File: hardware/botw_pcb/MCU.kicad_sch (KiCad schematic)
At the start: 12 parts, among them J1 Conn_02x03_Odd_Even, J2 Conn_01x03, U3 STM32F030CCTx, U4 MC6470

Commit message: Added pullups to I2C'
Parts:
- added R19, R20: 4k7, Resistor_SMD:R_0603_1608Metric, symbol Device:R_Small_US
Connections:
- net +3.3V: now also R19.2, R20.2
- net SCL: now also R19.1
- net SDA: now also R20.1
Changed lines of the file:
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@@
   (junction (at 180.34 71.12) (diameter 0) (color 0 0 0 0)
   )
+  (junction (at 218.44 134.62) (diameter 0) (color 0 0 0 0)
+  )
   (junction (at 167.64 71.12) (diameter 0) (color 0 0 0 0)
   )
@@
   (junction (at 135.89 139.7) (diameter 0) (color 0 0 0 0)
   )
-  (bus_entry (at 236.22 59.69) (size 2.54 2.54)
-    (stroke (width 0) (type default) (color 0 0 0 0))
-  )
   (bus_entry (at 519.43 19.05) (size 2.54 2.54)
     (stroke (width 0) (type default) (color 0 0 0 0))
@@
     (stroke (width 0) (type default) (color 0 0 0 0))
   )
+  (wire (pts (xy 218.44 134.62) (xy 218.44 137.16))
+    (stroke (width 0) (type default) (color 0 0 0 0))
+  )
+  (wire (pts (xy 222.25 130.81) (xy 222.25 134.62))
+    (stroke (width 0) (type default) (color 0 0 0 0))
+  )
   (wire (pts (xy 135.89 139.7) (xy 133.35 139.7))
     (stroke (width 0) (type default) (color 0 0 0 0))
@@
     (stroke (width 0) (type default) (color 0 0 0 0))
   )
+  (wire (pts (xy 218.44 133.35) (xy 218.44 134.62))
+    (stroke (width 0) (type default) (color 0 0 0 0))
+  )
   (wire (pts (xy 152.4 127) (xy 151.13 127))
     (stroke (width 0) (type default) (color 0 0 0 0))
@@
     (stroke (width 0) (type default) (color 0 0 0 0))
   )
+  (wire (pts (xy 218.44 134.62) (xy 222.25 134.62))
+    (stroke (width 0) (type default) (color 0 0 0 0))
+  )
   (wire (pts (xy 133.35 142.24) (xy 133.35 139.7))
     (stroke (width 0) (type default) (color 0 0 0 0))
@@
     )
   )
+  (global_label "SDA" (shape input) (at 213.36 137.16 180) (fields_autoplaced)
+    (effects (font (size 1.27 1.27)) (justify right))
+    (property "Intersheet References" "${INTERSHEET_REFS}" (id 0) (at 207.3788 137.0806 0)
+      (effects (font (size 1.27 1.27)) (justify right) hide)
+    )
+  )
   (global_label "SWDIO" (shape input) (at 189.23 123.19 0) (fields_autoplaced)
     (effects (font (size 1.27 1.27)) (justify left))
@@
     (effects (font (size 1.27 1.27)) (justify right))
     (property "Intersheet References" "${INTERSHEET_REFS}" (id 0) (at 108.1374 124.5394 0)
+      (effects (font (size 1.27 1.27)) (justify right) hide)
+    )
+  )
+  (global_label "SCL" (shape input) (at 213.36 133.35 180) (fields_autoplaced)
+    (effects (font (size 1.27 1.27)) (justify right))
+    (property "Intersheet References" "${INTERSHEET_REFS}" (id 0) (at 207.4393 133.4294 0)
       (effects (font (size 1.27 1.27)) (justify right) hide)
     )
@@
     (pin "1")
     (pin "2")
+  )
+  (symbol (lib_id "power:+3.3V") (at 222.25 130.81 0) (unit 1)
+    (in_bom yes) (on_board yes)
+    (property "Reference" "#PWR0153" (id 0) (at 222.25 134.62 0)
+      (effects (font (size 1.27 1.27)) hide)
+    )
+    (property "Value" "+3.3V" (id 1) (at 215.9 128.27 0)
+      (effects (font (size 1.27 1.27)) (justify left))
+    )
+    (property "Footprint" "" (id 2) (at 222.25 130.81 0)
+      (effects (font (size 1.27 1.27)) hide)
+    )
+    (property "Datasheet" "" (id 3) (at 222.25 130.81 0)
+      (effects (font (size 1.27 1.27)) hide)
+    )
+    (pin "1")
   )
   (symbol (lib_id "power:+3.3V") (at 243.84 111.76 0) (unit 1)
@@
     (pin "1")
   )
+  (symbol (lib_id "Device:R_Small_US") (at 215.9 137.16 90) (unit 1)
+    (in_bom yes) (on_board yes)
+    (property "Reference" "R20" (id 0) (at 215.9 142.24 90))
+    (property "Value" "4k7" (id 1) (at 215.9 139.7 90))
+    (property "Footprint" "Resistor_SMD:R_0603_1608Metric" (id 2) (at 215.9 137.16 0)
+      (effects (font (size 1.27 1.27)) hide)
+    )
+    (property "Datasheet" "~" (id 3) (at 215.9 137.16 0)
+      (effects (font (size 1.27 1.27)) hide)
+    )
+    (pin "1")
+    (pin "2")
+  )
   (symbol (lib_id "Device:R_Small_US") (at 102.87 104.14 0) (unit 1)
     (in_bom yes) (on_board yes) (fields_autoplaced)
@@
       (effects (font (size 1.27 1.27)) hide)
     )
+    (pin "1")
+    (pin "2")
+  )
+  (symbol (lib_id "Device:R_Small_US") (at 215.9 133.35 90) (unit 1)
+    (in_bom yes) (on_board yes) (fields_autoplaced)
+    (property "Reference" "R19" (id 0) (at 215.9 127 90))
+    (property "Value" "4k7" (id 1) (at 215.9 129.54 90))
+    (property "Footprint" "Resistor_SMD:R_0603_1608Metric" (id 2) (at 215.9 133.35 0)
+      (effects (font (size 1.27 1.27)) hide)
+    )
+    (property "Datasheet" "~" (id 3) (at 215.9 133.35 0)
+      (effects (font (size 1.27 1.27)) hide)
+    )

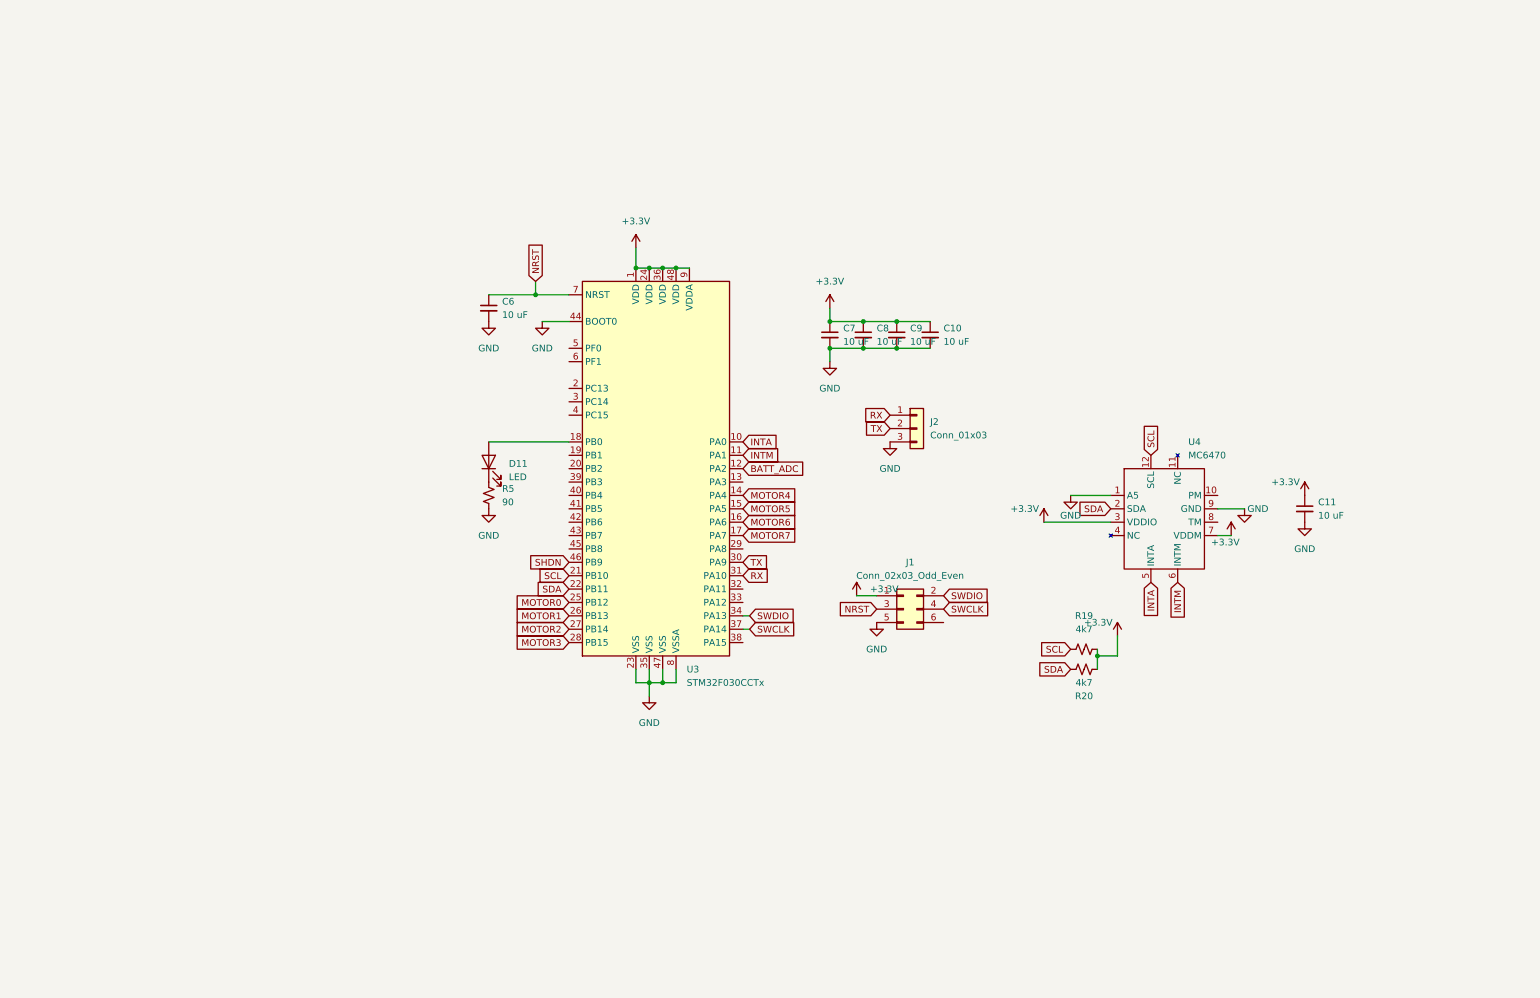
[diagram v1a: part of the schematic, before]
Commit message: Changed to a new part for mag
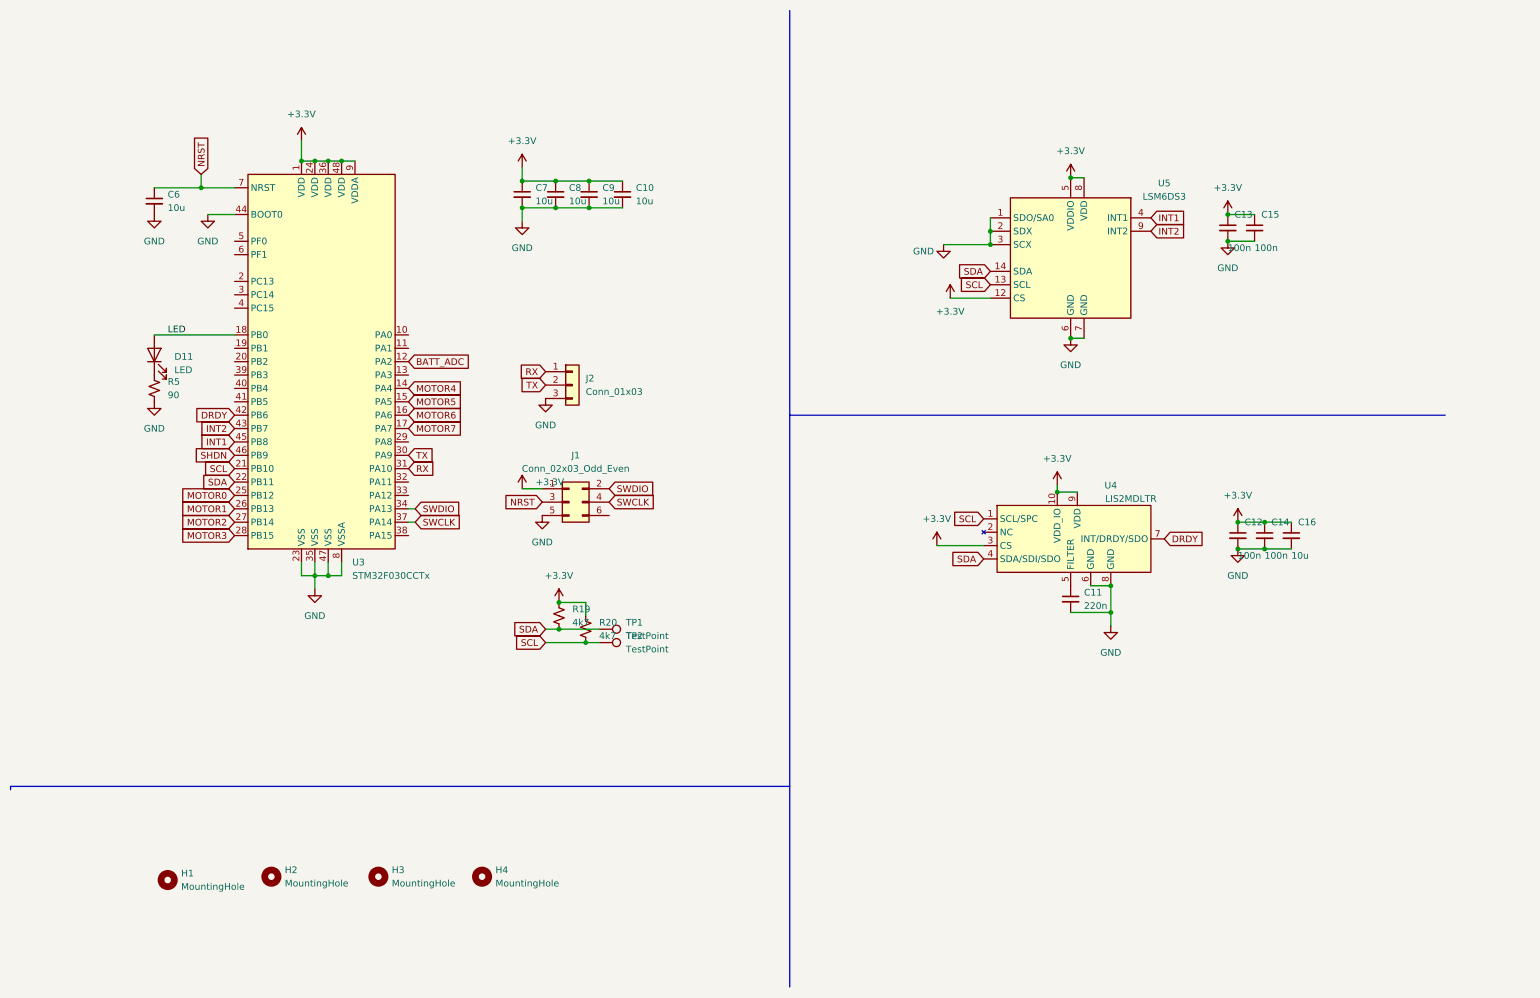
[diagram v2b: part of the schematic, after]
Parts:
- removed U4: MC6470, Package_LGA:LGA-12_2x2mm_P0.5mm, symbol custom:MC6470
- added C12, C13, C14, C15: 100n, Capacitor_SMD:C_0603_1608Metric, symbol Device:C_Small
- added C16: 10u, Capacitor_SMD:C_0603_1608Metric, symbol Device:C_Small
- added H1, H2, H3, H4: MountingHole, MountingHole:MountingHole_2.7mm_M2.5, symbol Mechanical:MountingHole
- added TP1, TP2: TestPoint, TestPoint:TestPoint_Pad_D1.0mm, symbol Connector:TestPoint
- added U4: LIS2MDLTR, Package_LGA:LGA-12_2x2mm_P0.5mm, symbol custom:LIS2MDLTR
- added U5: LSM6DS3, Package_LGA:LGA-14_3x2.5mm_P0.5mm_LayoutBorder3x4y, symbol Sensor_Motion:LSM6DS3
- C10, C6, C7, C8, C9: value 10 uF -> 10u
- C11: value 10 uF -> 220n
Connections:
- net +3.3V: now also R19.1, R20.1, C12.1, C13.1, C14.1, C15.1, C16.1, U4.10 (VDD_IO), U4.3 (CS), U4.9 (VDD), U5.12 (CS), U5.5 (VDDIO), U5.8 (VDD); no longer C11.1, R19.2, R20.2
- net GND: now also C12.2, C13.2, C14.2, C15.2, C16.2, U4.6 (GND), U4.8 (GND), U5.1 (SDO/SA0), U5.2 (SDX), U5.3 (SCX), U5.6 (GND), U5.7 (GND)
- net SCL: now also R20.2, TP2.1, U4.1 (SCL/SPC), U5.13 (SCL); no longer R19.1
- net SDA: now also R19.2, TP1.1, U4.4 (SDA/SDI/SDO), U5.14 (SDA); no longer R20.1
- net LED: now reaches D11.2 (A), U3.18 (PB0)
- net DRDY: now reaches U3.42 (PB6)
- net DRDY: now also U4.7 (INT/DRDY/SDO)
- net INT2: now reaches U3.43 (PB7)
- net INT2: now also U5.9 (INT2)
- net INT1: now reaches U3.45 (PB8)
- net INT1: now also U5.4 (INT1)
- net INTA: no longer names the net of U3.10 (PA0)
- net INTM: no longer names the net of U3.11 (PA1)
- new net: C11.1, U4.5 (FILTER)
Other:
- moved on the sheet: C10, C6, C7, C8, C9, D11, J1, J2, R5, U3
